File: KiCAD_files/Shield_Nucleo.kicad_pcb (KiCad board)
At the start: 4 copper layers, 100 x 100 mm, 145 parts, among them J1 Conn_01x02, J2 RJ45_LED_Shielded, J3 RJ45_LED_Shielded, J4 Conn_01x02_Male, J5 Conn_01x04_Male, J6 Conn_01x02, J8 Conn_02x07_Odd_Even, SW1 SW_Push, U1 STM32G474RE, U2 AT25xxx, U3 TCAN334GDR, U4 AP1117-33, U5 UCC21222DR, U6 UCC21222DR, U7 SFH617A-2X009T, Y1 NX3225SA-16.000000MHZ-T1

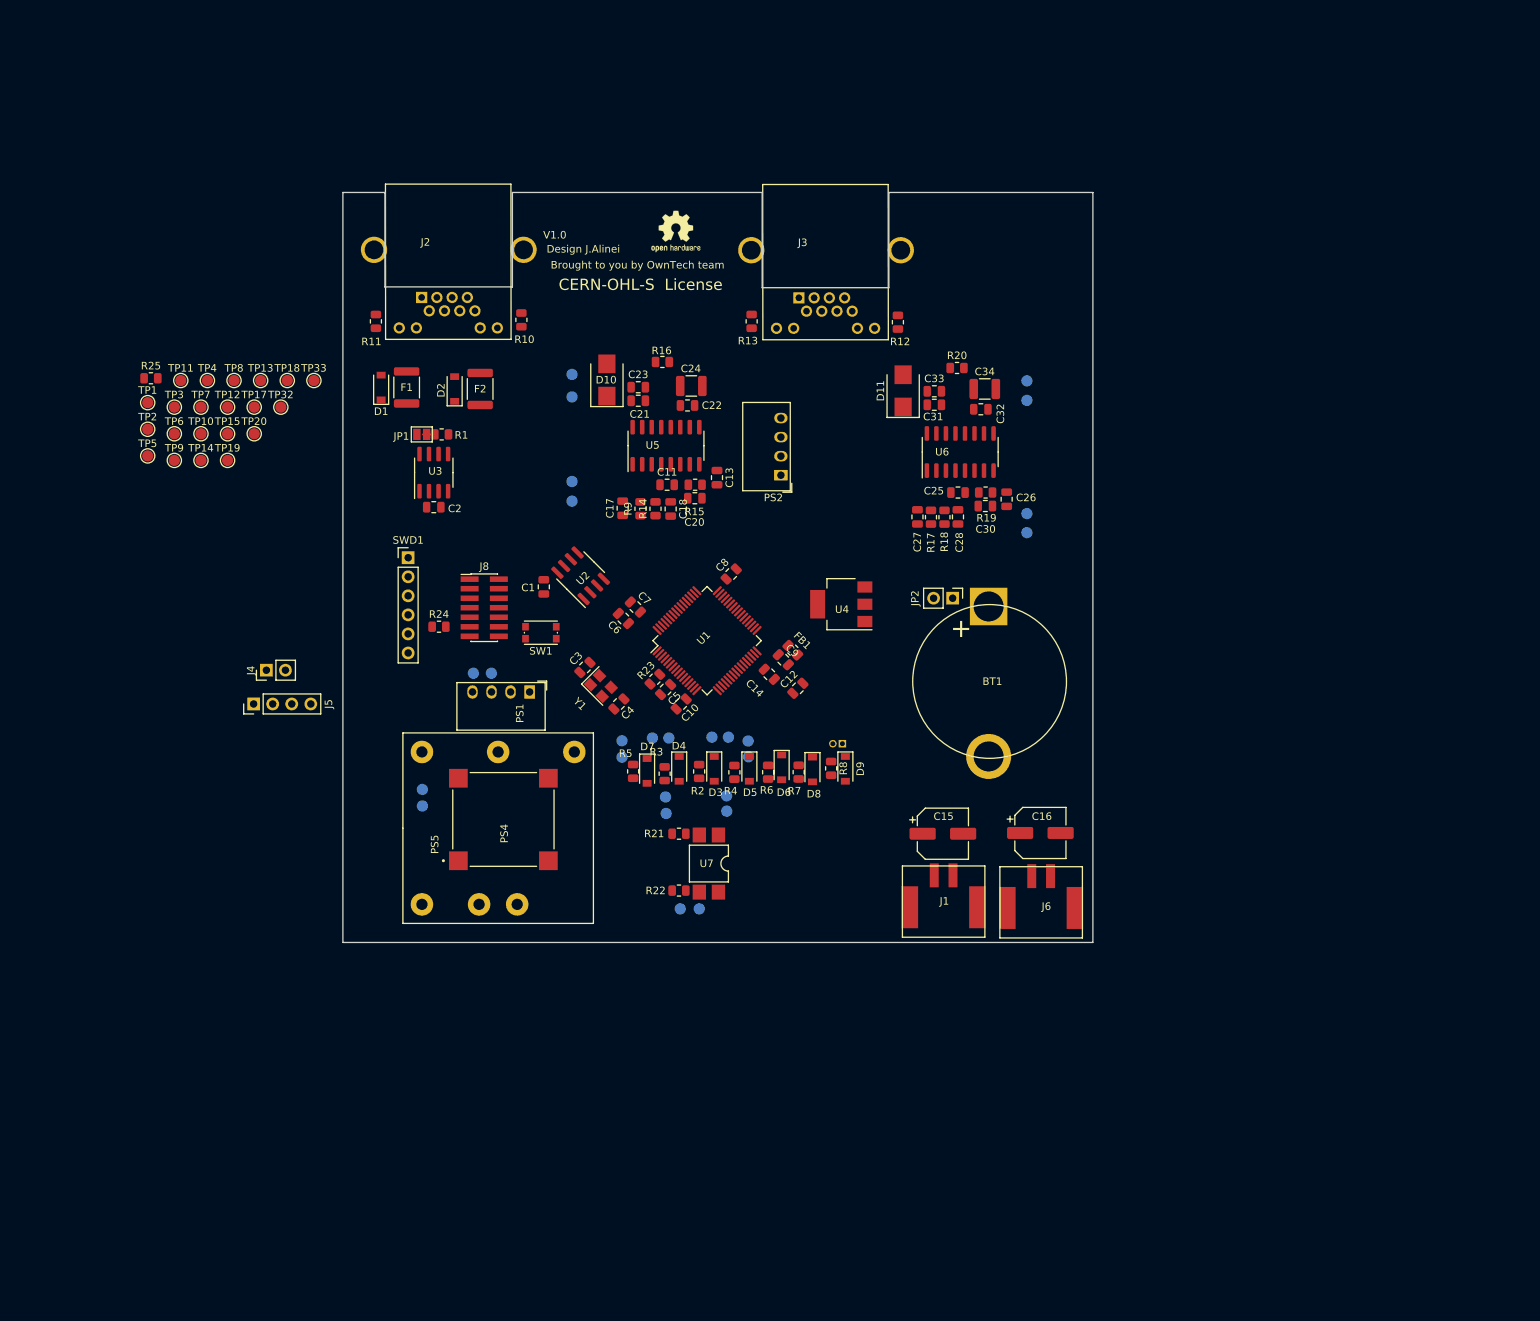
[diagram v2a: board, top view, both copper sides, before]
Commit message: WIP: Added pin positions in power footprint Mapped single ended adc on STM32, added feeder filter
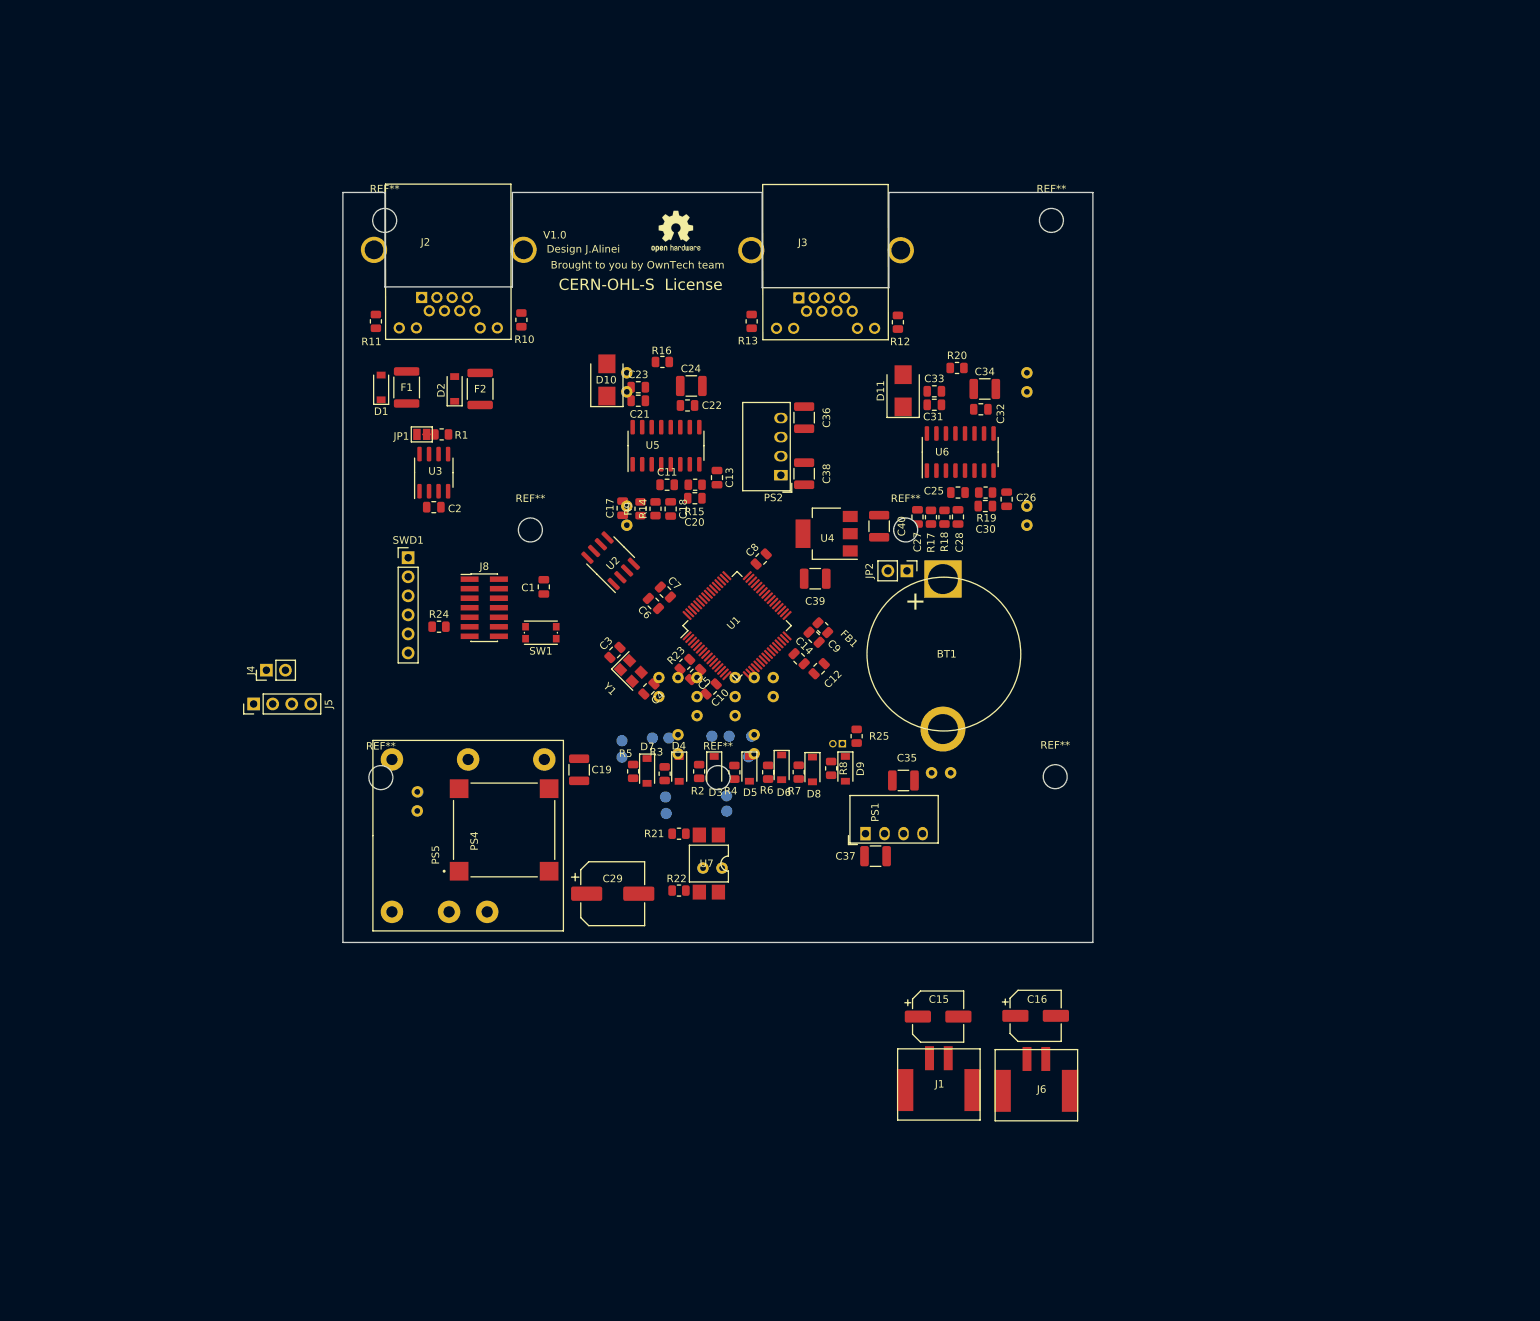
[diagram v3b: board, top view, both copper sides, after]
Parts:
- removed TP1, TP10, TP11, TP12, TP13, TP14, TP15, TP17, TP18, TP19, TP2, TP20, TP3, TP32, TP33, TP4, TP5, TP6, TP7, TP8, TP9: TestPoint, TestPoint:TestPoint_Pad_D1.5mm
- added C19: 10uF, Capacitor_SMD:C_1210_3225Metric, F.Cu at (70.0, 103.5)
- added C29: 10 to 47uF, Capacitor_SMD:CP_Elec_8x11.9, F.Cu at (74.5, 120.0)
- added C35: 10uF, Capacitor_SMD:C_1210_3225Metric, F.Cu at (113.2, 104.9)
- added C36: 10uF, Capacitor_SMD:C_1210_3225Metric, F.Cu at (100.0, 56.5)
- added C37: 10uF, Capacitor_SMD:C_1210_3225Metric, F.Cu at (109.5, 115.0)
- added C38: 10uF, Capacitor_SMD:C_1210_3225Metric, F.Cu at (100.0, 64.0)
- added C39: 10uF, Capacitor_SMD:C_1210_3225Metric, F.Cu at (101.5, 78.0)
- added C40: 10uF, Capacitor_SMD:C_1210_3225Metric, F.Cu at (110.0, 71.0)
- added REF**: MountingHole_3.2mm_M3, MountingHole:MountingHole_3.2mm_M3, F.Cu at (88.5, 104.5)
- added REF**: MountingHole_3.2mm_M3, MountingHole:MountingHole_3.2mm_M3, F.Cu at (43.6, 104.5)
- added REF**: MountingHole_3.2mm_M3, MountingHole:MountingHole_3.2mm_M3, F.Cu at (113.5, 71.5)
- added REF**: MountingHole_3.2mm_M3, MountingHole:MountingHole_3.2mm_M3, F.Cu at (63.5, 71.5)
- added REF**: MountingHole_3.2mm_M3, MountingHole:MountingHole_3.2mm_M3, F.Cu at (44.1, 30.2)
- added REF**: MountingHole_3.2mm_M3, MountingHole:MountingHole_3.2mm_M3, F.Cu at (133.0, 30.2)
- added REF**: MountingHole_3.2mm_M3, MountingHole:MountingHole_3.2mm_M3, F.Cu at (133.5, 104.4)
- moved R25 105.5 mm to (107.0, 99.0), turned to 90 degrees
- moved TP46 62.6 mm to (119.5, 103.9)
- moved TP47 62.5 mm to (117.0, 103.9)
- moved PS1 48.6 mm to (108.2, 112.0), turned to 90 degrees
- moved J1 24.4 mm to (118.0, 146.2)
- moved C15 24.4 mm to (117.9, 136.4)
- moved C16 24.4 mm to (130.9, 136.3)
- moved J6 24.4 mm to (131.0, 146.3)
- moved U4 9.60 mm to (103.0, 72.0)
- moved TP26 7.98 mm to (76.3, 68.3)
- moved TP43 7.95 mm to (76.3, 70.9)
- moved TP31 7.31 mm to (76.3, 53.1)
- moved TP24 7.28 mm to (76.3, 50.5)
- moved BT1 7.10 mm to (118.5, 88.0)
- moved JP2 7.10 mm to (113.7, 76.9)
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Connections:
- net /V2_low_N renamed Net-(U1-Pad21)
- net /V2_low_P renamed Net-(U1-Pad20)
- net /V_high_N renamed Net-(U1-Pad26)
- net /V_high_P renamed Net-(U1-Pad23)
- D5 pad 1: /I1_low_mcu -> /I2_low_mcu
- D9 pad 1: /Temp -> /Temp_mcu
- R4 pad 1: /I1_low_mcu -> /I2_low_mcu
- R8 pad 1: /Temp -> /Temp_mcu
- U1 pad 10: /I_high -> /I_high_mcu
- U1 pad 12: /V1_low_P -> /V1_low_mcu
- U1 pad 13: /V1_low_N -> /V2_low_mcu
- U1 pad 19: Net-(U1-Pad19) -> /V_high_mcu
- U1 pad 25: /Temp -> /Temp_mcu
- U1 pad 8: /I1_low -> /I1_low_mcu
- U1 pad 9: /I2_low -> /I2_low_mcu

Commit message: WIP: improved the power footprint. Adapted component placement acoordingly
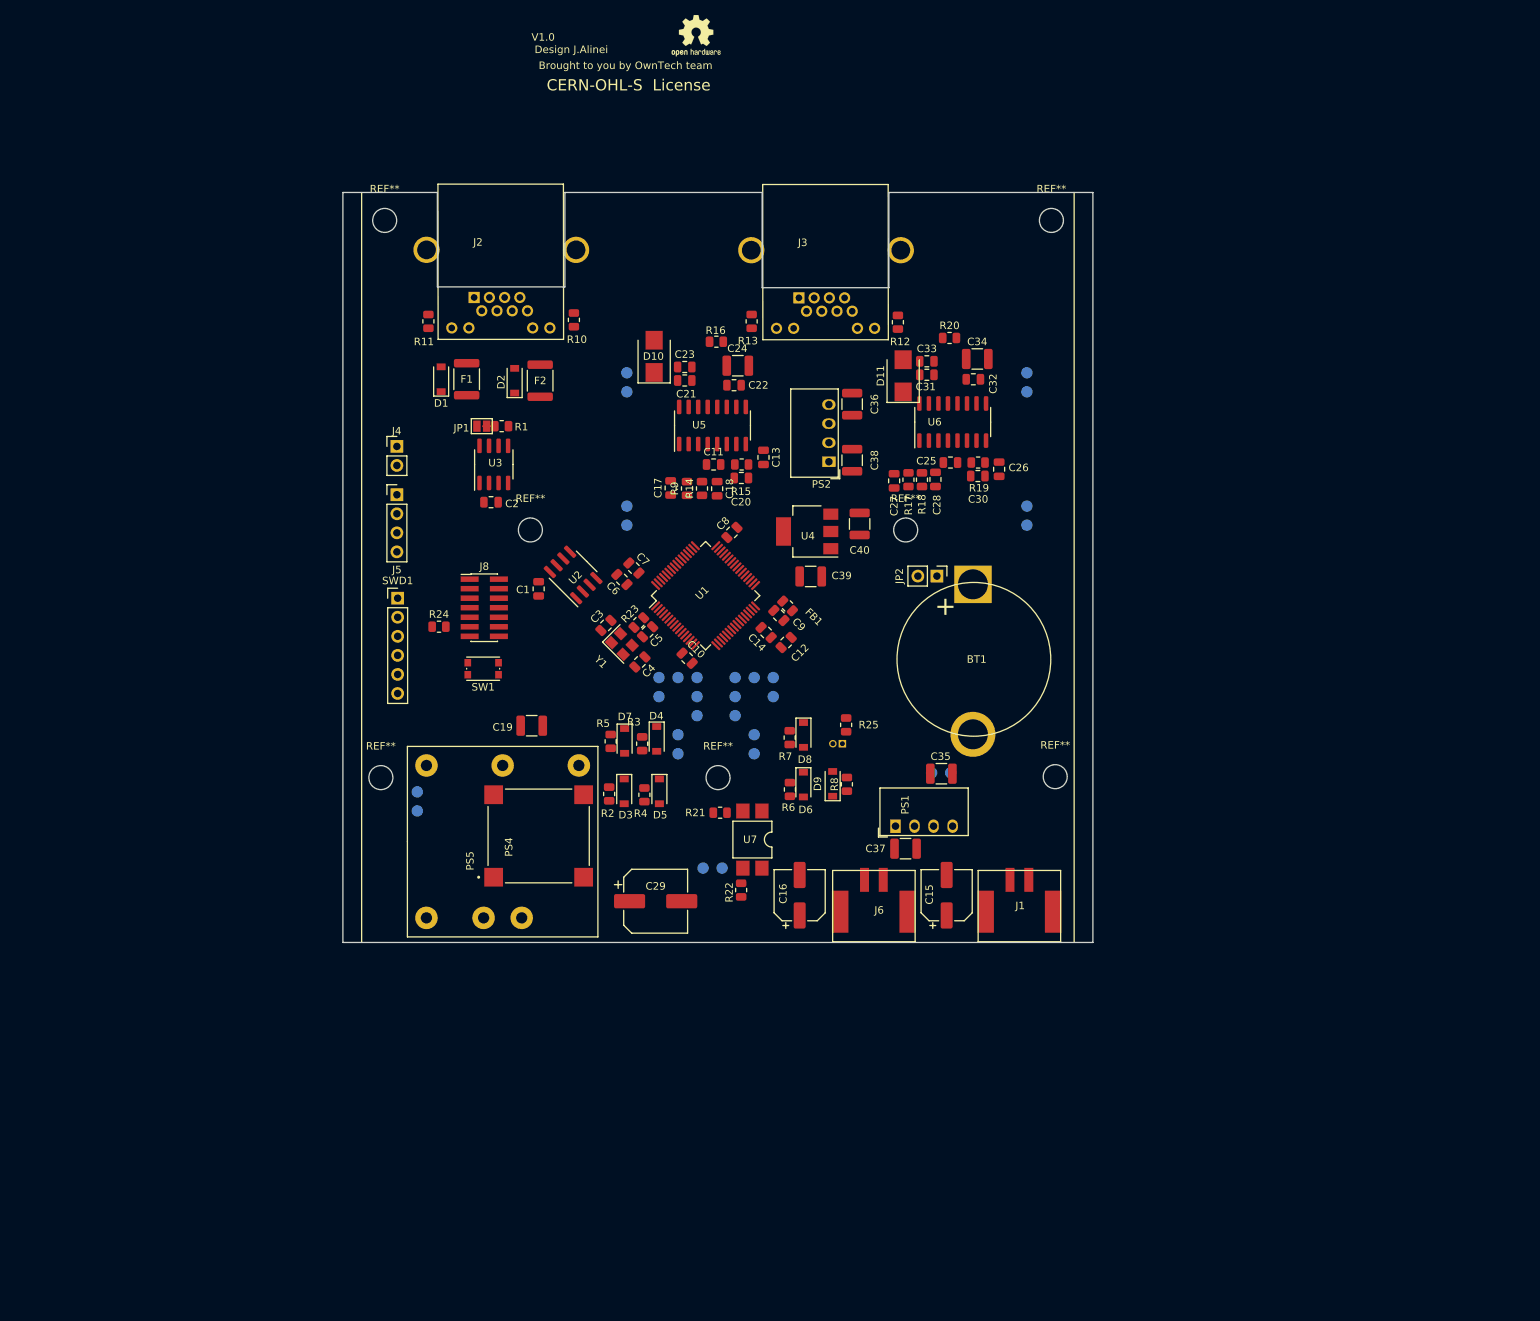
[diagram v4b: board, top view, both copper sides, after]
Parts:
- removed TP16, TP21, TP22, TP23, TP24, TP25, TP26, TP27, TP28, TP29, TP30, TP31, TP34, TP35, TP36, TP37, TP38, TP39, TP40, TP41, TP42, TP43, TP44, TP45, TP46, TP47: TestPoint, TestPoint:TestPoint_Pad_D1.5mm
- moved C16 35.3 mm to (99.4, 120.2), turned to 90 degrees
- moved J4 34.5 mm to (45.7, 60.4), turned to 0 degrees
- moved J5 33.8 mm to (45.7, 66.8), turned to 0 degrees
- moved J6 32.2 mm to (109.3, 122.4)
- moved REF** 26.2 mm to (85.6, 5.60)
- moved J1 26.1 mm to (128.7, 122.4)
- moved C15 16.2 mm to (119.0, 120.2), turned to 90 degrees
- moved D3 12.4 mm to (76.0, 106.3)
- moved D5 12.4 mm to (80.7, 106.3)
- moved R2 12.4 mm to (74.0, 106.7)
- moved R4 12.4 mm to (78.7, 106.8)
- moved SW1 9.07 mm to (57.2, 90.0)
- moved C19 8.63 mm to (63.7, 97.6), turned to 180 degrees
- moved C5 8.57 mm to (79.1, 85.1)
- moved R22 8.29 mm to (91.6, 119.5), turned to 90 degrees
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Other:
- outline, holes or cut-outs redrawn
